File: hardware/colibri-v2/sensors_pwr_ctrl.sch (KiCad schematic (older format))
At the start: 2 parts

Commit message: added wnd_lcd.sch
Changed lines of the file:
@@
 $Descr A4 11693 8268
 encoding utf-8
-Sheet 11 22
+Sheet 10 23
 Title ""
 Date ""
@@
 	6500 3750 6500 3450
 Wire Wire Line
-	3250 3950 5600 3950
-Wire Wire Line
-	5600 3950 6200 3950
+	3250 3950 6200 3950
 $Comp
 L R R?

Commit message: Annotated Components
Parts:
- gave numbers to parts that had none: 2
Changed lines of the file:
@@
 $EndDescr
 $Comp
-L +3V3 #PWR?
+L +3V3 #PWR76
 U 1 1 55FF262C
 P 6500 3450
-F 0 "#PWR?" H 6500 3300 50  0001 C CNN
+F 0 "#PWR76" H 6500 3300 50  0001 C CNN
 F 1 "+3V3" H 6500 3590 50  0000 C CNN
 F 2 "" H 6500 3450 60  0000 C CNN
@@
 $EndComp
 $Comp
-L Q_PMOS_GSD Q?
+L Q_PMOS_GSD Q6
 U 1 1 55FF2632
 P 6400 3950
-F 0 "Q?" H 6700 4000 50  0000 R CNN
+F 0 "Q6" H 6700 4000 50  0000 R CNN
 F 1 "Q_PMOS_GSD" H 7050 3900 50  0000 R CNN
 F 2 "" H 6600 4050 29  0000 C CNN
@@
 	3250 3950 6200 3950
 $Comp
-L R R?
+L R R56
 U 1 1 55FF263D
 P 5600 4350
-F 0 "R?" V 5680 4350 50  0000 C CNN
+F 0 "R56" V 5680 4350 50  0000 C CNN
 F 1 "10K" V 5600 4350 50  0000 C CNN
 F 2 "" V 5530 4350 30  0000 C CNN
@@
 $EndComp
 $Comp
-L GND #PWR?
+L GND #PWR75
 U 1 1 55FF2644
 P 5600 4700
-F 0 "#PWR?" H 5600 4450 50  0001 C CNN
+F 0 "#PWR75" H 5600 4450 50  0001 C CNN
 F 1 "GND" H 5600 4550 50  0000 C CNN
 F 2 "" H 5600 4700 60  0000 C CNN

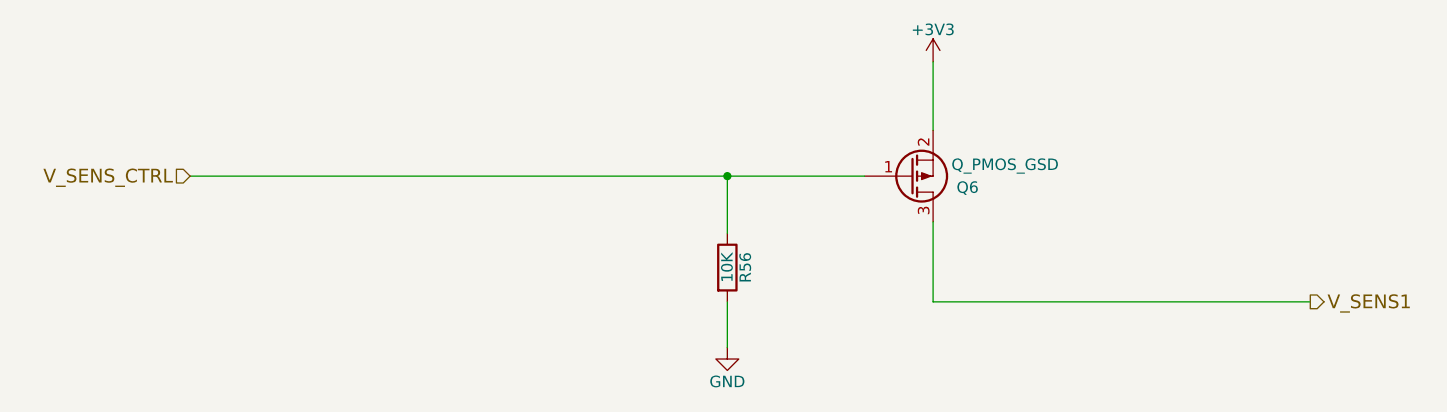
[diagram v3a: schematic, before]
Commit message: Separate VDD_IO
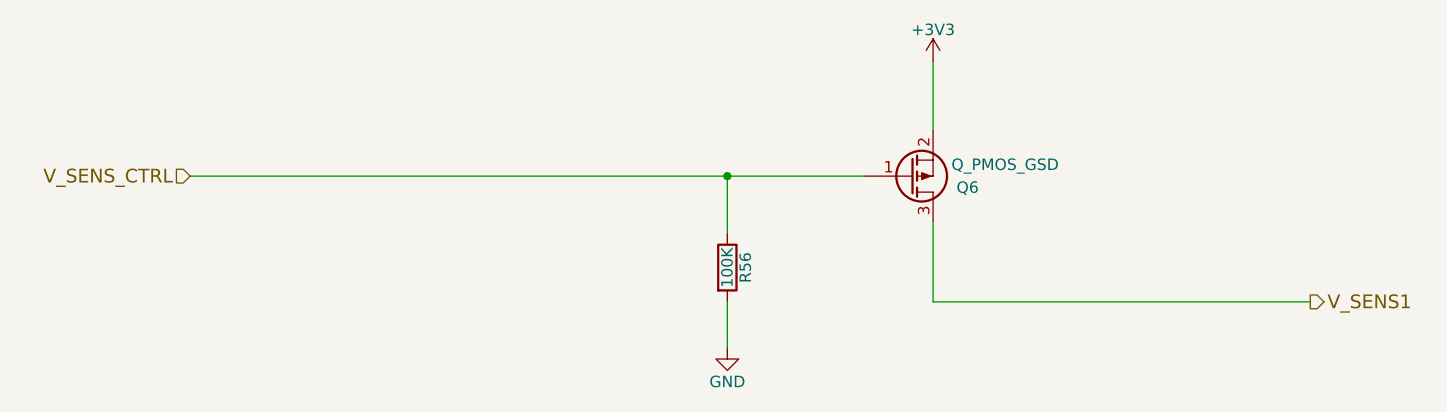
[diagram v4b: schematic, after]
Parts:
- R56: value 10K -> 100K
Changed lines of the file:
@@
 P 5600 4350
 F 0 "R56" V 5680 4350 50  0000 C CNN
-F 1 "10K" V 5600 4350 50  0000 C CNN
+F 1 "100K" V 5600 4350 50  0000 C CNN
 F 2 "" V 5530 4350 30  0000 C CNN
 F 3 "" H 5600 4350 30  0000 C CNN

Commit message: Re-annotated schematic
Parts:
- renumbered R56 to R57
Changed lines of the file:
@@
 $EndDescr
 $Comp
-L +3V3 #PWR077
+L +3V3 #PWR73
 U 1 1 55FF262C
 P 6500 3450
-F 0 "#PWR077" H 6500 3300 50  0001 C CNN
+F 0 "#PWR73" H 6500 3300 50  0001 C CNN
 F 1 "+3V3" H 6500 3590 50  0000 C CNN
 F 2 "" H 6500 3450 60  0000 C CNN
@@
 	3250 3950 6200 3950
 $Comp
-L R R56
+L R R57
 U 1 1 55FF263D
 P 5600 4350
-F 0 "R56" V 5680 4350 50  0000 C CNN
+F 0 "R57" V 5680 4350 50  0000 C CNN
 F 1 "100K" V 5600 4350 50  0000 C CNN
 F 2 "" V 5530 4350 30  0000 C CNN
@@
 $EndComp
 $Comp
-L GND #PWR078
+L GND #PWR72
 U 1 1 55FF2644
 P 5600 4700
-F 0 "#PWR078" H 5600 4450 50  0001 C CNN
+F 0 "#PWR72" H 5600 4450 50  0001 C CNN
 F 1 "GND" H 5600 4550 50  0000 C CNN
 F 2 "" H 5600 4700 60  0000 C CNN

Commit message: Associated footprints for R and some of the C
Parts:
- R57: footprint (none) -> Resistors_SMD:R_0603
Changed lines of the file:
@@
 $EndDescr
 $Comp
-L +3V3 #PWR73
+L +3V3 #PWR074
 U 1 1 55FF262C
 P 6500 3450
-F 0 "#PWR73" H 6500 3300 50  0001 C CNN
+F 0 "#PWR074" H 6500 3300 50  0001 C CNN
 F 1 "+3V3" H 6500 3590 50  0000 C CNN
 F 2 "" H 6500 3450 60  0000 C CNN
@@
 F 0 "Q6" H 6700 4000 50  0000 R CNN
 F 1 "Q_PMOS_GSD" H 7050 3900 50  0000 R CNN
-F 2 "" H 6600 4050 29  0000 C CNN
+F 2 "" H 6600 4050 29  0001 C CNN
 F 3 "" H 6400 3950 60  0000 C CNN
 	1    6400 3950
@@
 F 0 "R57" V 5680 4350 50  0000 C CNN
 F 1 "100K" V 5600 4350 50  0000 C CNN
-F 2 "" V 5530 4350 30  0000 C CNN
+F 2 "Resistors_SMD:R_0603" V 5530 4350 30  0001 C CNN
 F 3 "" H 5600 4350 30  0000 C CNN
 	1    5600 4350
@@
 $EndComp
 $Comp
-L GND #PWR72
+L GND #PWR075
 U 1 1 55FF2644
 P 5600 4700
-F 0 "#PWR72" H 5600 4450 50  0001 C CNN
+F 0 "#PWR075" H 5600 4450 50  0001 C CNN
 F 1 "GND" H 5600 4550 50  0000 C CNN
 F 2 "" H 5600 4700 60  0000 C CNN

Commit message: Work on cortex USB connection.
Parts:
- removed R57: 100K, Resistors_SMD:R_0603, symbol R
- added R?: 100K/5%, Resistors_SMD:R_0603, symbol R_SMT
- renumbered Q6 to Q?
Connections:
- net GND: now also R?.2
- net V_SENS_CTRL: now also R?.1
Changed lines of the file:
@@
 $EndDescr
 $Comp
-L +3V3 #PWR074
+L +3V3 #PWR?
 U 1 1 55FF262C
 P 6500 3450
-F 0 "#PWR074" H 6500 3300 50  0001 C CNN
+F 0 "#PWR?" H 6500 3300 50  0001 C CNN
 F 1 "+3V3" H 6500 3590 50  0000 C CNN
 F 2 "" H 6500 3450 60  0000 C CNN
@@
 $EndComp
 $Comp
-L Q_PMOS_GSD Q6
+L Q_PMOS_GSD Q?
 U 1 1 55FF2632
 P 6400 3950
-F 0 "Q6" H 6700 4000 50  0000 R CNN
+F 0 "Q?" H 6700 4000 50  0000 R CNN
 F 1 "Q_PMOS_GSD" H 7050 3900 50  0000 R CNN
 F 2 "" H 6600 4050 29  0001 C CNN
@@
 	3250 3950 6200 3950
 $Comp
-L R R57
-U 1 1 55FF263D
-P 5600 4350
-F 0 "R57" V 5680 4350 50  0000 C CNN
-F 1 "100K" V 5600 4350 50  0000 C CNN
-F 2 "Resistors_SMD:R_0603" V 5530 4350 30  0001 C CNN
-F 3 "" H 5600 4350 30  0000 C CNN
-	1    5600 4350
-	1    0    0    -1
-$EndComp
-$Comp
-L GND #PWR075
+L GND #PWR?
 U 1 1 55FF2644
 P 5600 4700
-F 0 "#PWR075" H 5600 4450 50  0001 C CNN
+F 0 "#PWR?" H 5600 4450 50  0001 C CNN
 F 1 "GND" H 5600 4550 50  0000 C CNN
 F 2 "" H 5600 4700 60  0000 C CNN
@@
 Text HLabel 3250 3950 0    60   Input ~ 0
 V_SENS_CTRL
+$Comp
+L R_SMT R?
+U 1 1 562EF326
+P 5600 4350
+F 0 "R?" V 5670 4350 50  0000 C CNN
+F 1 "100K/5%" V 5530 4350 50  0000 C CNN
+F 2 "Resistors_SMD:R_0603" V 5750 4350 30  0001 C CNN
+F 3 "" V 5680 4350 30  0000 C CNN
+F 4 "0603" V 5600 4350 20  0000 C CNN "SMT"
+F 5 "9233628" V 5800 4350 30  0001 C CNN "Part"
+F 6 "Farnell" V 5850 4350 30  0001 C CNN "Provider"
+	1    5600 4350
+	1    0    0    -1
+$EndComp
 $EndSCHEMATC
